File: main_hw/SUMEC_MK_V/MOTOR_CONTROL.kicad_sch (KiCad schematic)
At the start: 19 parts, among them IC2 DRV8874PWPR, IC3 DRV8874PWPR, J2 Conn_01x06_Socket, J3 Conn_01x06_Socket

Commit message: 67yfhtgftu
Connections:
- net EN_L: now also IC2.1 (EN/IN1); no longer IC3.1 (EN/IN1)
- net EN_R: now also IC3.1 (EN/IN1); no longer IC2.1 (EN/IN1)
- net MOTOR_L_1: now also IC2.8 (OUT1), J2.6 (Pin_6); no longer IC3.8 (OUT1), J3.6 (Pin_6)
- net MOTOR_L_2: now also IC2.10 (OUT2), J2.5 (Pin_5); no longer IC3.10 (OUT2), J3.5 (Pin_5)
- net MOTOR_R_1: now also IC3.8 (OUT1), J3.6 (Pin_6); no longer IC2.8 (OUT1), J2.6 (Pin_6)
- net MOTOR_R_2: now also IC3.10 (OUT2), J3.5 (Pin_5); no longer IC2.10 (OUT2), J2.5 (Pin_5)
- net OUT_L_A: now also J2.3 (Pin_3); no longer J3.3 (Pin_3)
- net OUT_L_B: now also J2.2 (Pin_2); no longer J3.2 (Pin_2)
- net OUT_R_A: now also J3.3 (Pin_3); no longer J2.3 (Pin_3)
- net OUT_R_B: now also J3.2 (Pin_2); no longer J2.2 (Pin_2)
- net PH_L: now also IC2.2 (PH/IN2); no longer IC3.2 (PH/IN2)
- net PH_R: now also IC3.2 (PH/IN2); no longer IC2.2 (PH/IN2)
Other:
- note added: "RIGHT"

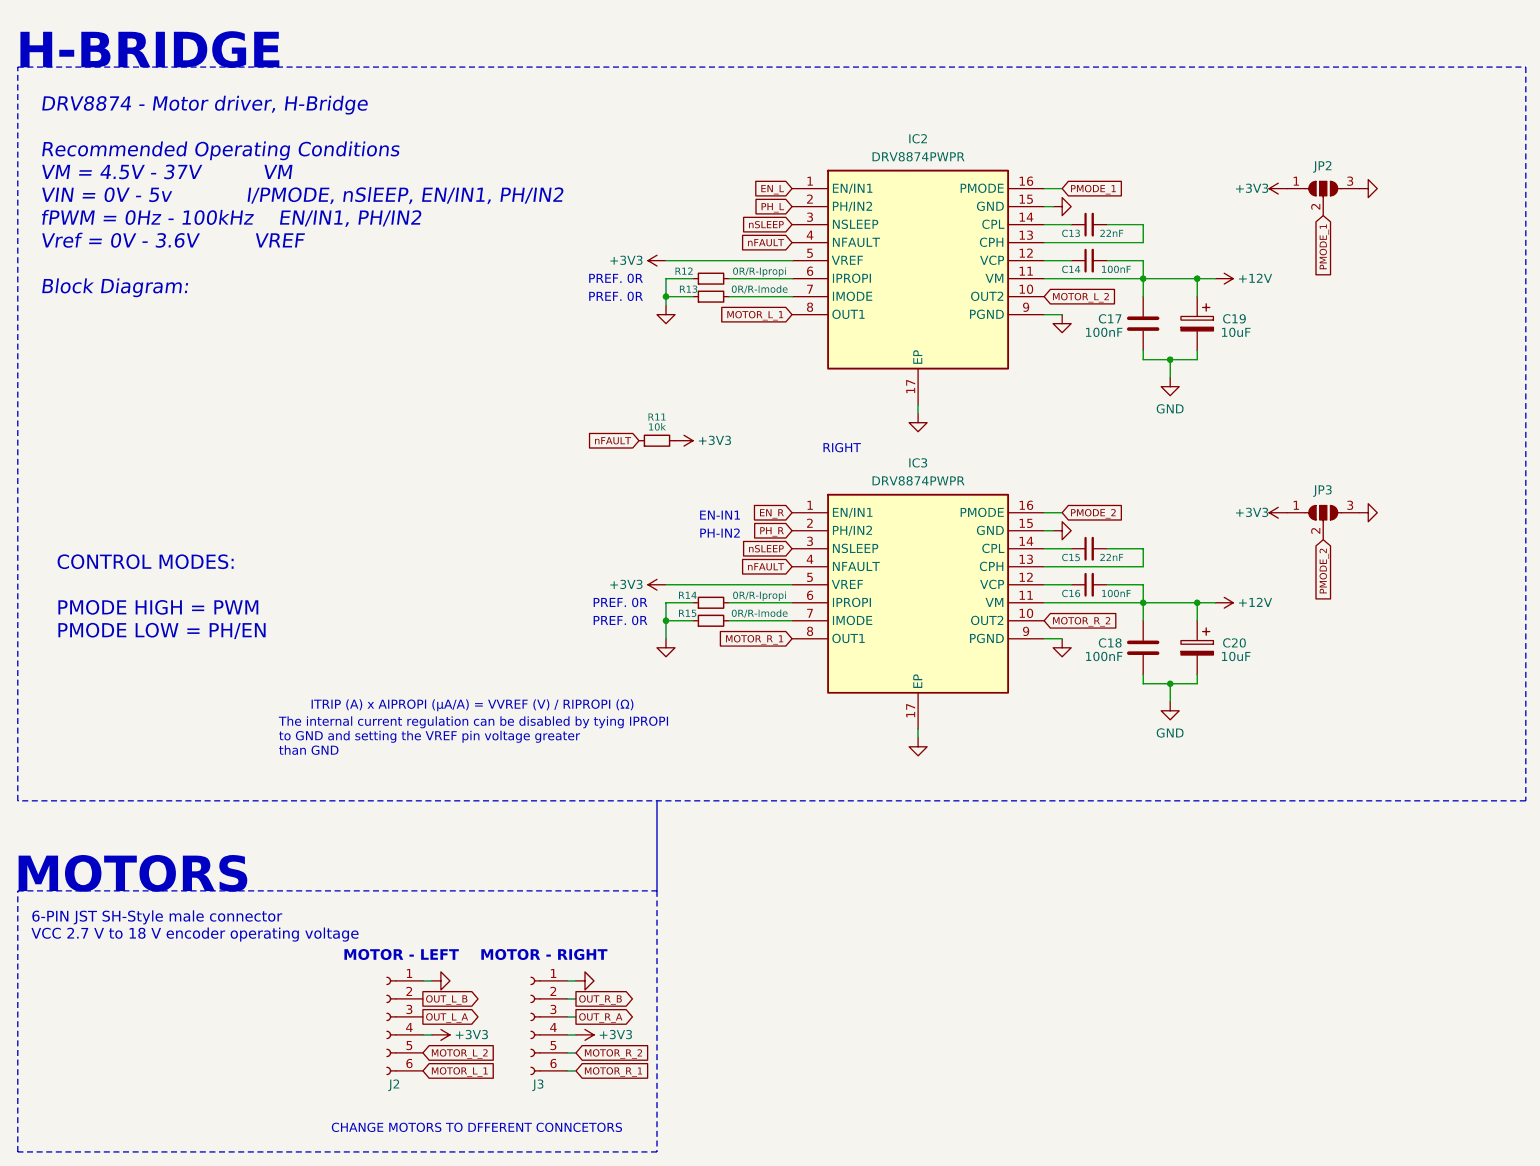
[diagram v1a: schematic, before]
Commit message: MK5 bugfix fixed POL_L, minor changes, deleted nSLEEP and nFault connections to the MCU
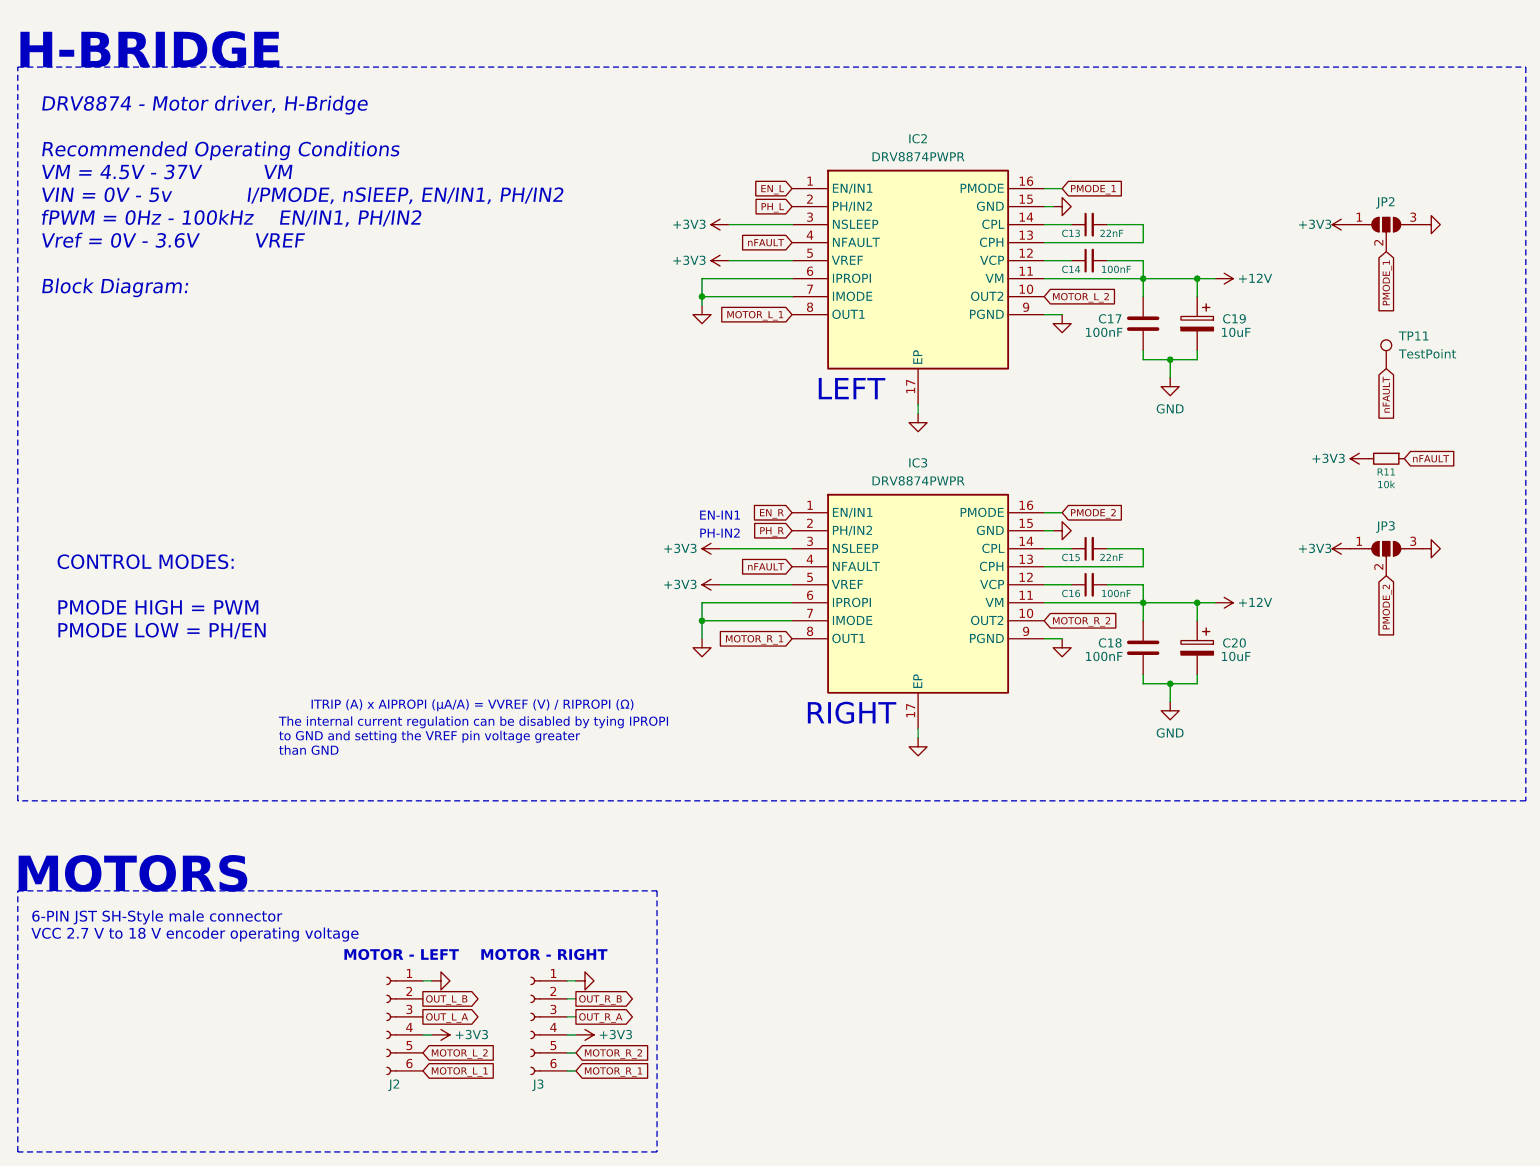
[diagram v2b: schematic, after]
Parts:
- removed R12, R14: 0R/R-Ipropi, Resistor_SMD:R_0805_2012Metric_Pad1.20x1.40mm_HandSolder, symbol Device:R_Small
- removed R13, R15: 0R/R-Imode, Resistor_SMD:R_0805_2012Metric_Pad1.20x1.40mm_HandSolder, symbol Device:R_Small
- added TP11: TestPoint, TestPoint:TestPoint_Pad_D1.0mm, symbol Connector:TestPoint
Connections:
- net nSLEEP is gone; now on net +3V3: IC2.3 (NSLEEP), IC3.3 (NSLEEP)
- net GND: now also IC2.6 (IPROPI), IC2.7 (IMODE), IC3.6 (IPROPI), IC3.7 (IMODE)
- net nFAULT: now also TP11.1
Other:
- note added: "LEFT"
- note removed: "CHANGE MOTORS TO DFFERENT CONNCETORS"
- note removed: "PREF. 0R"
- moved on the sheet: JP2, JP3, R11

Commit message: updates to mk5
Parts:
- renumbered C13 to C12, C14 to C13, C15 to C14, C16 to C15, C17 to C16, C18 to C17, C19 to C18, C20 to C19, R11 to R10

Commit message: MK5 PCB rework
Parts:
- removed C12, C14: 22nF, Capacitor_SMD:C_0805_2012Metric_Pad1.18x1.45mm_HandSolder, symbol Device:C_Small
- removed C13, C15: 100nF, Capacitor_SMD:C_0805_2012Metric_Pad1.18x1.45mm_HandSolder, symbol Device:C_Small
- removed C16, C17: 100nF, Capacitor_SMD:C_0805_2012Metric_Pad1.18x1.45mm_HandSolder, symbol Device:C
- removed C18, C19: 10uF, Capacitor_Tantalum_SMD:CP_EIA-3216-18_Kemet-A_Pad1.58x1.35mm_HandSolder, symbol Device:C_Polarized
- removed IC2, IC3: DRV8874PWPR, sumec_brd:DRV8874, symbol sumec_sch_lib:DRV8874PWPR
- removed J2, J3: Conn_01x06_Socket, Connector_JST:JST_SH_BM06B-SRSS-TB_1x06-1MP_P1.00mm_Vertical, symbol Connector:Conn_01x06_Socket
- removed JP2, JP3: SolderJumper_3_Open, Jumper:SolderJumper-3_P2.0mm_Open_TrianglePad1.0x1.5mm, symbol Jumper:SolderJumper_3_Open
- removed R10: 10k, Resistor_SMD:R_0805_2012Metric_Pad1.20x1.40mm_HandSolder, symbol Device:R_Small
- removed TP11: TestPoint, TestPoint:TestPoint_Pad_D1.0mm, symbol Connector:TestPoint
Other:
- note removed: "6-PIN JST SH-Style male connector VCC 2.7 V to 18 V encoder operating voltage"
- note removed: "CONTROL MODES: PMODE HIGH = PWM PMODE LOW = PH/EN"
- note removed: "DRV8874 - Motor driver, H-Bridge Recommended Operating Conditions VM = 4.5V - 37V VM VIN = 0V - 5v I/PMODE, nSlEEP, EN/IN1, PH/IN2 fPWM = 0Hz - 100kHz EN/IN1, PH/IN2 Vref = 0V - 3.6V VREF Block Diagram:"
- note removed: "EN-IN1"
- note removed: "H-BRIDGE"
- note removed: "ITRIP (A) x AIPROPI (μA/A) = VVREF (V) / RIPROPI (Ω)"
- note removed: "LEFT"
- note removed: "MOTOR - LEFT"
- note removed: "MOTOR - RIGHT"
- note removed: "MOTORS"
- note removed: "PH-IN2"
- note removed: "RIGHT"
- note removed: "The internal current regulation can be disabled by tying IPROPI to GND and setting the VREF pin voltage greater than GND"
